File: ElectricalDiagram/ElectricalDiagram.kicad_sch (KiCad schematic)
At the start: 26 parts

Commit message: Prepped Electrical Diagram for meeting
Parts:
- removed U11: ~, symbol Robomaster_Library:C620 Motor Speed Controller
- removed U13: ~, symbol Robomaster_Library:M3508
- removed U26: ~, symbol Robomaster_Library:PMM
- removed U3: ~, symbol Robomaster_Library:VTM
- removed U4: ~, symbol Robomaster_Library:SMM
- added U11: ~, symbol Robomaster_Library:M3508
- added U13: ~, symbol Robomaster_Library:C620 Motor Speed Controller
- added U26: ~, symbol Robomaster_Library:Dev_Board
- added U27: ~, symbol Robomaster_Library:Power Management Module
- added U28: ~, symbol Robomaster_Library:TB47/TB48S
- added U29: ~, symbol Robomaster_Library:Main Control Module
- added U3: ~, symbol Robomaster_Library:Video Transmitter Module
- added U4: ~, symbol Robomaster_Library:Speed Monitor Module
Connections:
- net at U12. (Phase_3): now also U10. (TX)
- net at U16. (Phase_3): now also U17. (TX)
- net at U25. (TX): now also U24. (Phase_3)
- net at U8. (Phase_3): now also U9. (TX)
- net at U22. (Phase_3): now also U23. (TX)
- net at U1. (USB): now also U2. (USB_Realsense)
- net at U20. (Phase_3): now also U21. (TX)
- net at U5. (Phase_3): now also U7. (TX)
- net at U14. (Phase_3): now also U15. (TX)
- net at U18. (Phase_3): now also U19. (TX)
- new net: U10. (TX), U12. (Phase_3) (x3)
- new net: U5. (Phase_3), U7. (TX) (x3)
- new net: U11. (Phase_3), U13. (TX) (x4)
- new net: U14. (Phase_3), U15. (TX) (x3)
- new net: U24. (Phase_3), U25. (TX) (x3)
- new net: U27. (SYS_SMO3B_2), U28. (GND) (x2)
- new net: U3. (UART_TX), U4. (Ref_Out)
- new net: U8. (Phase_3), U9. (TX) (x3)
- new net: U22. (Phase_3), U23. (TX) (x3)
- new net: U20. (Phase_3), U21. (TX) (x3)
- new net: U27. (SYS_SMO3B_2), U29. (Ref_PMM)
- new net: U16. (Phase_3), U17. (TX) (x3)
- new net: U18. (Phase_3), U19. (TX) (x3)
- no-connect marks 0 -> 1
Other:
- removed sheet Slipring
- note added: "Back Left Drivepod"
- note added: "Back Right Drivepod"
- note added: "Barrel Assembly"
- note added: "Chassis-Side"
- note added: "Feeder"
- note added: "Front Left Drivepod"
- note added: "Front Right Drivepod"
- note added: "Left Flywheel"
- note added: "Pitch"
- note added: "Right Flywheel"
- note added: "Turret-Side"
- note added: "Waterwheel"
- note added: "Yaw 1"
- note added: "Yaw 2"

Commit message: Added hierarchial labels to chassis board, please look over
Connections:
- net at U10. (TX): no longer U12. (Phase_3)
- net at U7. (TX): no longer U5. (Phase_3)
- net at U13. (TX): no longer U11. (Phase_3)
- net at U15. (TX): now also U14. (Phase_3)
- net at U25. (TX): now also U24. (Phase_3)
- net at U27. (SYS_SMO3B_2): no longer U28. (GND)
- net at U3. (UART_TX): now also U4. (Ref_Out)
- net at U4. (Ref_Out): no longer U3. (UART_TX)
- net at U9. (TX): no longer U8. (Phase_3)
- net at U23. (TX): no longer U22. (Phase_3)
- net at U21. (TX): no longer U20. (Phase_3)
- net at U17. (TX): now also U16. (Phase_3)
- net at U19. (TX): no longer U18. (Phase_3)
- new net: U10. (TX), U12. (Phase_3) (x3)
- new net: U5. (Phase_3), U7. (TX) (x3)
- new net: U11. (Phase_3), U13. (TX) (x3)
- new net: U14. (Phase_3), U15. (TX) (x3)
- new net: U24. (Phase_3), U25. (TX) (x3)
- new net: U27. (SYS_SMO3B_2), U28. (GND)
- new net: U8. (Phase_3), U9. (TX) (x3)
- new net: U22. (Phase_3), U23. (TX) (x3)
- new net: U20. (Phase_3), U21. (TX) (x3)
- new net: U16. (Phase_3), U17. (TX) (x3)
- new net: U18. (Phase_3), U19. (TX) (x3)
- now unconnected: U10. (TX), U10. (TX), U13. (TX), U13. (TX), U19. (TX), U19. (TX), U21. (TX), U21. (TX), U23. (TX), U23. (TX), U7. (TX), U7. (TX), U9. (TX), U9. (TX)
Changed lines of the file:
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@@
 	)
 	(symbol
-		(lib_name "Robomaster_Library:M3508")
 		(lib_id "Robomaster_Library:M3508")
 		(at 24.13 30.48 0)
@@
 	)
 	(symbol
-		(lib_name "Robomaster_Library:M3508")
 		(lib_id "Robomaster_Library:M3508")
 		(at 187.96 64.77 0)
@@
 	)
 	(symbol
-		(lib_name "Robomaster_Library:M3508")
 		(lib_id "Robomaster_Library:M3508")
 		(at 24.13 53.34 0)
@@
 	)
 	(symbol
-		(lib_name "Robomaster_Library:C620 Motor Speed Controller")
 		(lib_id "Robomaster_Library:C620 Motor Speed Controller")
 		(at 59.69 203.2 0)
@@
 	)
 	(symbol
-		(lib_name "Robomaster_Library:C620 Motor Speed Controller")
 		(lib_id "Robomaster_Library:C620 Motor Speed Controller")
 		(at 72.39 172.72 0)
@@
 	)
 	(symbol
-		(lib_name "Robomaster_Library:M3508")
 		(lib_id "Robomaster_Library:M3508")
 		(at 46.99 170.18 0)
@@
 	)
 	(symbol
-		(lib_name "Robomaster_Library:M3508")
 		(lib_id "Robomaster_Library:M3508")
 		(at 187.96 88.9 0)
@@
 	)
 	(symbol
-		(lib_name "Robomaster_Library:M3508")
 		(lib_id "Robomaster_Library:M3508")
 		(at 163.83 170.18 0)
@@
 	)
 	(symbol
-		(lib_name "Robomaster_Library:C620 Motor Speed Controller")
 		(lib_id "Robomaster_Library:C620 Motor Speed Controller")
 		(at 162.56 91.44 0)
@@
 	)
 	(symbol
-		(lib_name "Robomaster_Library:M3508")
 		(lib_id "Robomaster_Library:M3508")
 		(at 177.8 231.14 0)
@@
 	)
 	(symbol
-		(lib_name "Robomaster_Library:C620 Motor Speed Controller")
 		(lib_id "Robomaster_Library:C620 Motor Speed Controller")
 		(at 162.56 67.31 0)
@@
 	)
 	(symbol
-		(lib_name "Robomaster_Library:M3508")
 		(lib_id "Robomaster_Library:M3508")
 		(at 34.29 200.66 0)
@@
 	)
 	(symbol
-		(lib_name "Robomaster_Library:C620 Motor Speed Controller")
 		(lib_id "Robomaster_Library:C620 Motor Speed Controller")
 		(at 49.53 55.88 0)
@@
 	)
 	(symbol
-		(lib_name "Robomaster_Library:C620 Motor Speed Controller")
 		(lib_id "Robomaster_Library:C620 Motor Speed Controller")
 		(at 49.53 33.02 0)
@@
 	)
 	(symbol
-		(lib_name "Robomaster_Library:C620 Motor Speed Controller")
 		(lib_id "Robomaster_Library:C620 Motor Speed Controller")
 		(at 59.69 233.68 0)
@@
 	)
 	(symbol
-		(lib_name "Robomaster_Library:M3508")
 		(lib_id "Robomaster_Library:M3508")
 		(at 177.8 200.66 0)
@@
 	)
 	(symbol
-		(lib_name "Robomaster_Library:M3508")
 		(lib_id "Robomaster_Library:M3508")
 		(at 34.29 231.14 0)
@@
 	)
 	(symbol
-		(lib_name "Robomaster_Library:C620 Motor Speed Controller")
 		(lib_id "Robomaster_Library:C620 Motor Speed Controller")
 		(at 152.4 233.68 0)
@@
 	)
 	(symbol
-		(lib_name "Robomaster_Library:C620 Motor Speed Controller")
 		(lib_id "Robomaster_Library:C620 Motor Speed Controller")
 		(at 152.4 203.2 0)
@@
 	)
 	(symbol
-		(lib_name "Robomaster_Library:C620 Motor Speed Controller")
 		(lib_id "Robomaster_Library:C620 Motor Speed Controller")
 		(at 138.43 172.72 0)

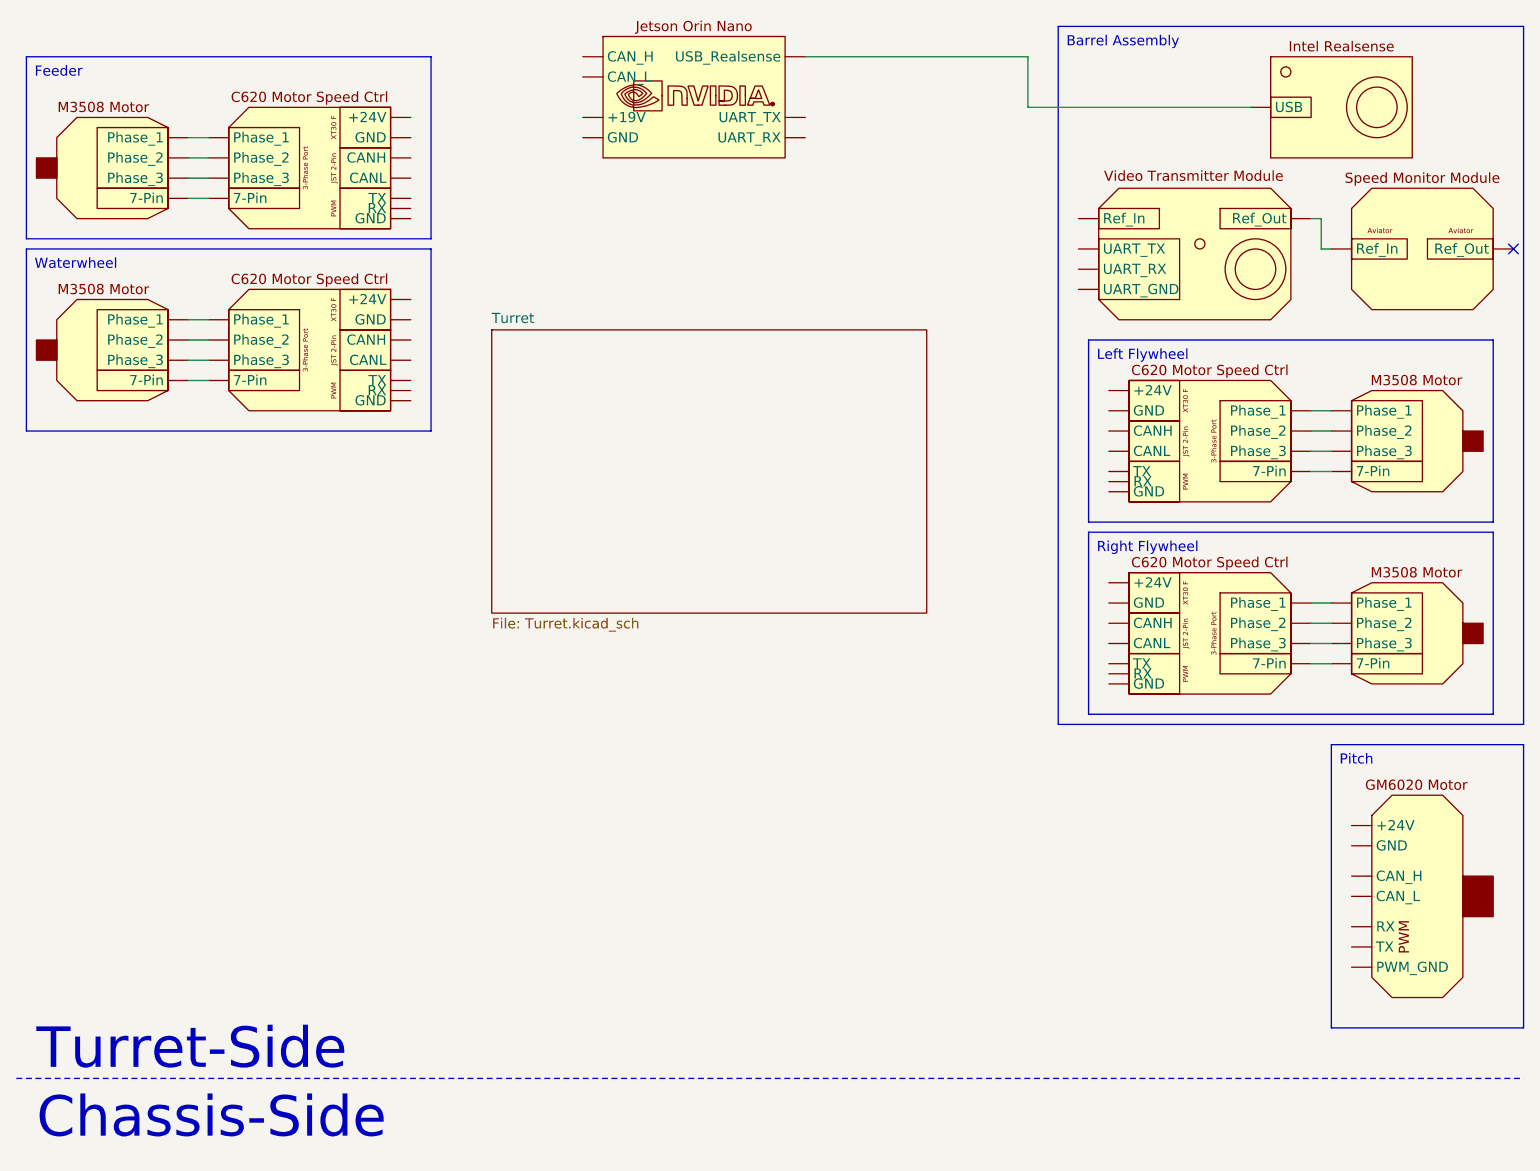
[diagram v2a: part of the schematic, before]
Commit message: Updated diagram w/ new turret schematic
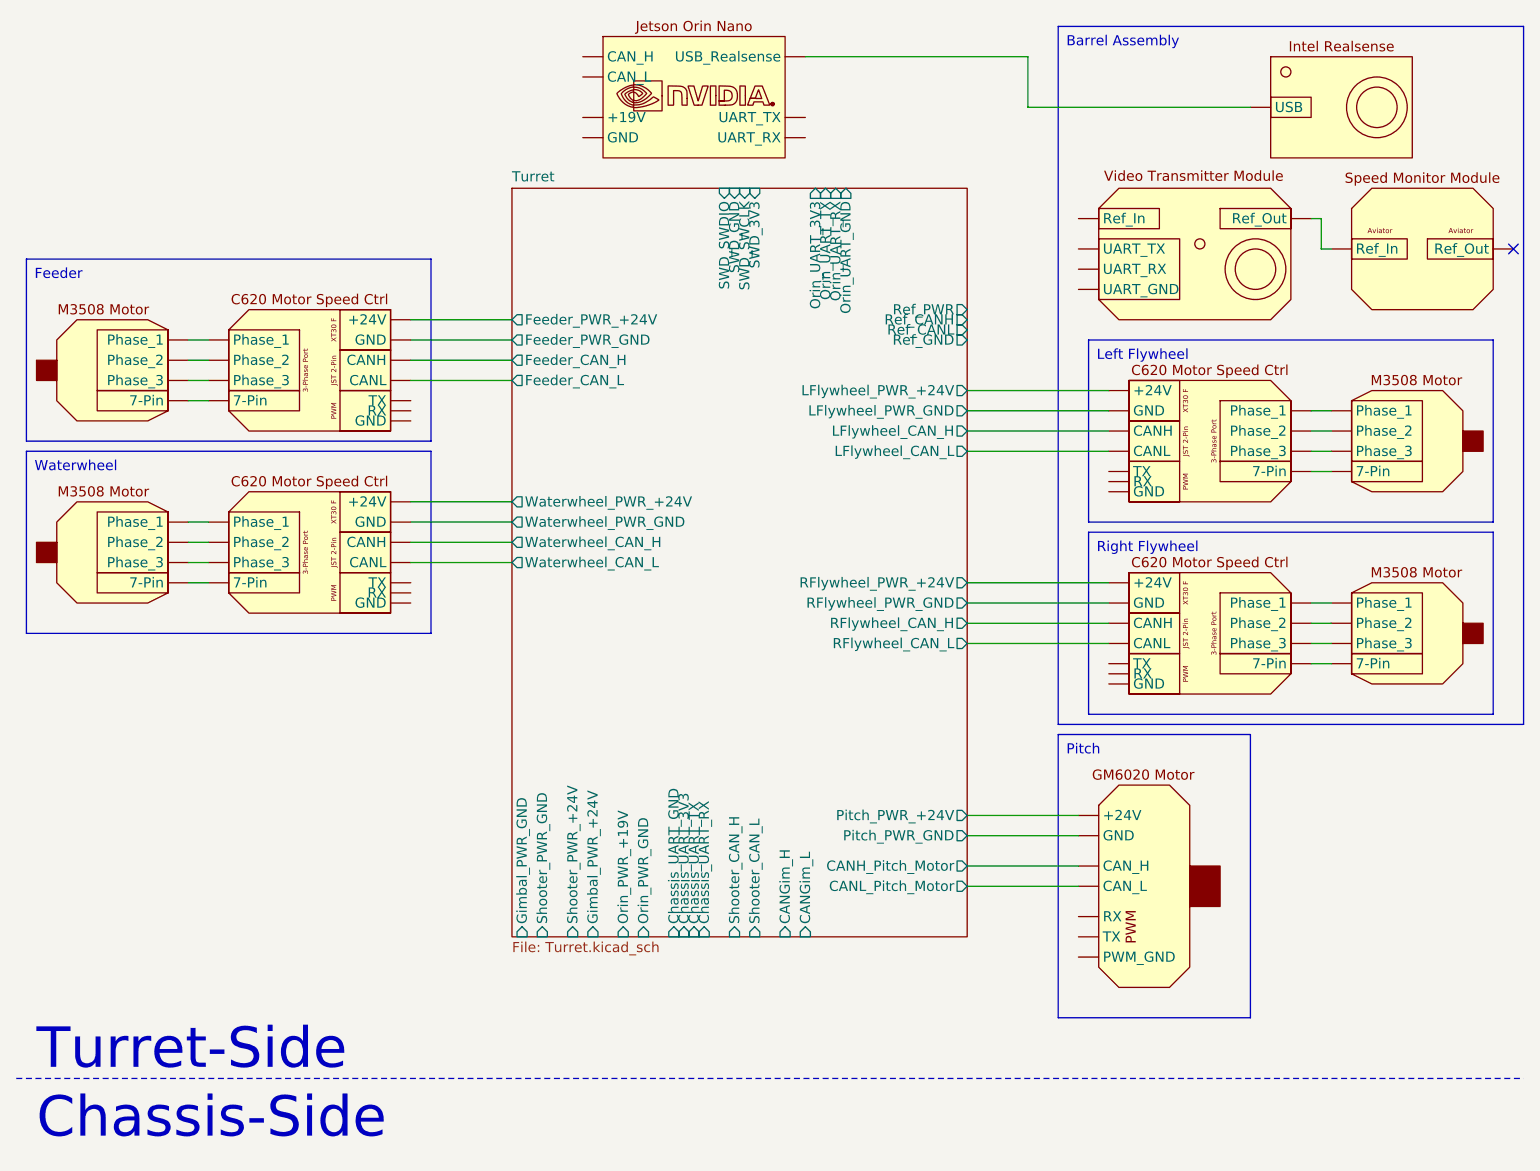
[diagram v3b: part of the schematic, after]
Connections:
- net Turret/Feeder_PWR_GND: now reaches U10. (TX)
- net Turret/Feeder_PWR_GND: no longer U12. (Phase_3)
- net Turret/LFlywheel_PWR_GND: now reaches U7. (TX)
- net Turret/LFlywheel_PWR_GND: no longer U5. (Phase_3)
- net Turret/Waterwheel_PWR_GND: now reaches U13. (TX)
- net Turret/Waterwheel_PWR_GND: no longer U11. (Phase_3)
- net at U15. (TX): now also U14. (Phase_3)
- net at U25. (TX): now also U24. (Phase_3)
- net at U27. (SYS_SMO3B_2): no longer U28. (GND)
- net Turret/Pitch_PWR_GND: now reaches U6. (TX)
- net at U3. (UART_TX): now also U4. (Ref_Out)
- net at U4. (Ref_Out): no longer U3. (UART_TX)
- net Turret/RFlywheel_PWR_GND: now reaches U9. (TX)
- net Turret/RFlywheel_PWR_GND: no longer U8. (Phase_3)
- net at U23. (TX): no longer U22. (Phase_3)
- net at U21. (TX): no longer U20. (Phase_3)
- net at U17. (TX): now also U16. (Phase_3)
- net at U19. (TX): no longer U18. (Phase_3)
- new net: U10. (TX), U12. (Phase_3) (x3)
- new net: U5. (Phase_3), U7. (TX) (x3)
- new net: U11. (Phase_3), U13. (TX) (x3)
- new net: U14. (Phase_3), U15. (TX) (x3)
- new net: U24. (Phase_3), U25. (TX) (x3)
- new net: U27. (SYS_SMO3B_2), U28. (GND)
- new net: U8. (Phase_3), U9. (TX) (x3)
- new net: U22. (Phase_3), U23. (TX) (x3)
- new net: U20. (Phase_3), U21. (TX) (x3)
- new net: U16. (Phase_3), U17. (TX) (x3)
- new net: U18. (Phase_3), U19. (TX) (x3)
- new net Turret/CANH_Pitch_Motor: U6. (TX)
- new net Turret/CANL_Pitch_Motor: U6. (TX)
- new net Turret/Feeder_CAN_H: U10. (TX)
- new net Turret/Feeder_CAN_L: U10. (TX)
- new net Turret/Feeder_PWR_+24V: U10. (TX)
- new net Turret/LFlywheel_CAN_H: U7. (TX)
- new net Turret/LFlywheel_CAN_L: U7. (TX)
- new net Turret/LFlywheel_PWR_+24V: U7. (TX)
- new net Turret/Pitch_PWR_+24V: U6. (TX)
- new net Turret/RFlywheel_CAN_H: U9. (TX)
- new net Turret/RFlywheel_CAN_L: U9. (TX)
- new net Turret/RFlywheel_PWR_+24V: U9. (TX)
- new net Turret/Waterwheel_CAN_H: U13. (TX)
- new net Turret/Waterwheel_CAN_L: U13. (TX)
- new net Turret/Waterwheel_PWR_+24V: U13. (TX)
- now unconnected: U19. (TX), U19. (TX), U21. (TX), U21. (TX), U23. (TX), U23. (TX)
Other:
- sheet Turret ports: added CANGim_H, CANGim_L, CANH_Pitch_Motor, CANL_Pitch_Motor, Chassis_UART_3V3, Chassis_UART_GND, Chassis_UART_RX, Chassis_UART_TX, Feeder_CAN_H, Feeder_CAN_L, Feeder_PWR_+24V, Feeder_PWR_GND, Gimbal_PWR_+24V, Gimbal_PWR_GND, LFlywheel_CAN_H, LFlywheel_CAN_L, LFlywheel_PWR_+24V, LFlywheel_PWR_GND, Orin_PWR_+19V, Orin_PWR_GND, Orin_UART_3V3, Orin_UART_GND, Orin_UART_RX, Orin_UART_TX, Pitch_PWR_+24V, Pitch_PWR_GND, RFlywheel_CAN_H, RFlywheel_CAN_L, RFlywheel_PWR_+24V, RFlywheel_PWR_GND, Ref_CANH, Ref_CANL, Ref_GND, Ref_PWR, SWD_3V3, SWD_GND, SWD_SWCLK, SWD_SWDIO, Shooter_CAN_H, Shooter_CAN_L, Shooter_PWR_+24V, Shooter_PWR_GND, Waterwheel_CAN_H, Waterwheel_CAN_L, Waterwheel_PWR_+24V, Waterwheel_PWR_GND; removed none
